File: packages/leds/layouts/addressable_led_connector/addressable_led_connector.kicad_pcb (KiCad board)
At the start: 2 copper layers, 1 part

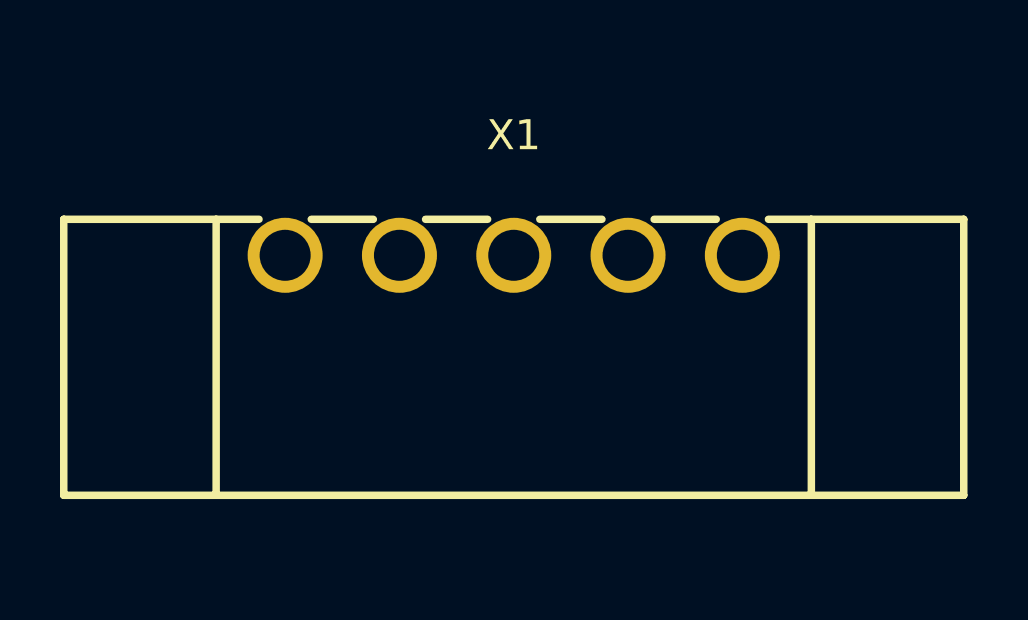
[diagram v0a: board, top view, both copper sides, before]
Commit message: Remove connectors and replace with leds package
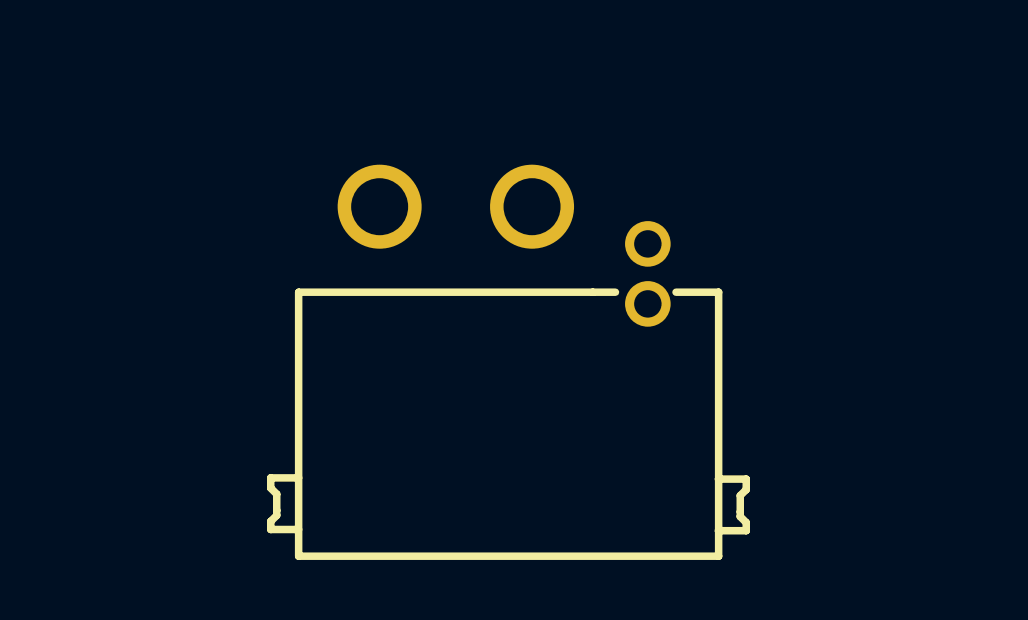
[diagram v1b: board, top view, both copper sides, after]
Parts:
- removed X1: , atopile:CONN-TH_5P-P3.81_DB2ERM-3.81-5P-6a82d0
- added U1: , atopile:CONN-TH_4P-XT30PW-M-e6a65c, F.Cu at (0.00, 0.00)

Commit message: [Publish] Rebuild modules (with no dep on upstream atopile pr) (#5)
* Fixes image link on published packages
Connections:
- U1 pad 3: line -> line-1
- U1 pad 4: line-1 -> line
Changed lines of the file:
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@@
     )
     (net 0 "")
-    (net 1 "line")
+    (net 1 "line-1")
     (net 2 "gnd")
-    (net 3 "line-1")
+    (net 3 "line")
     (net 4 "hv")
     (footprint "atopile:CONN-TH_4P-XT30PW-M-e6a65c"
@@
             (drill 0.9144)
             (layers "*.Cu" "*.Mask")
-            (net 1 "line")
+            (net 1 "line-1")
         )
         (pad "4" thru_hole circle
@@
             (drill 0.9144)
             (layers "*.Cu" "*.Mask")
-            (net 3 "line-1")
+            (net 3 "line")
         )
     )

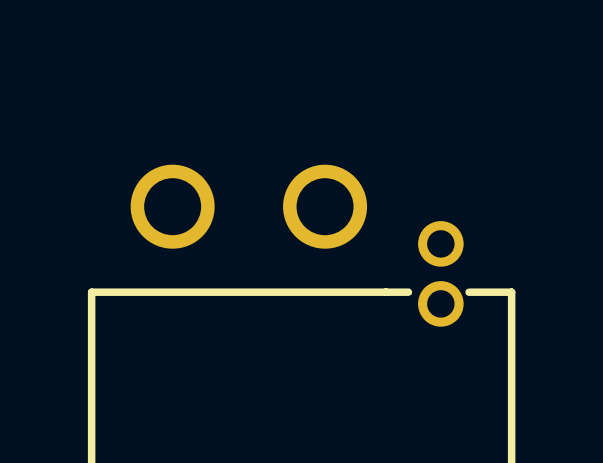
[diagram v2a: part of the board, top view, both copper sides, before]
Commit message: Add various addressable LEDs
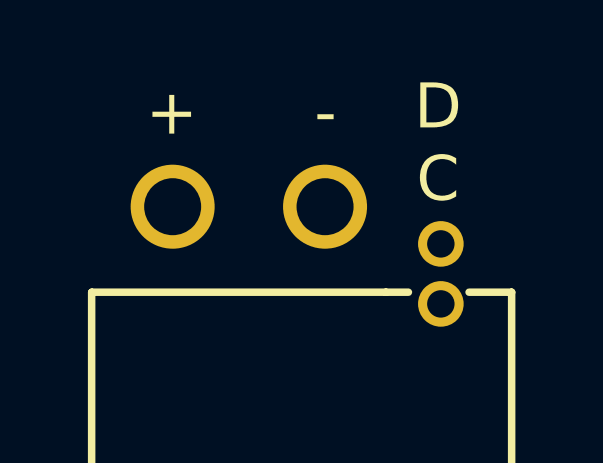
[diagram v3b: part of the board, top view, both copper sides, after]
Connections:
- U1 pad 3: line-1 -> line
- U1 pad 4: line -> line-1
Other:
- board text added: "+"
- board text added: "-"
- board text added: "D C"
